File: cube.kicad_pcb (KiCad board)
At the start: 2 copper layers, 282 parts, among them J1 serial_conn, J2 shifters_common_conn, U1 SN74HC595N_0_b, U10 SN74HC595N_3_b, U11 SN74HC595N_3_g, U12 SN74HC595N_3_r, U13 SN74HC595N_4_b, U14 SN74HC595N_4_g, U15 SN74HC595N_4_r, U16 SN74HC595N_5_b, U17 SN74HC595N_5_g, U18 SN74HC595N_5_r, U19 SN74HC595N_6_b, U2 SN74HC595N_0_g, U20 SN74HC595N_6_g, U21 SN74HC595N_6_r, U22 SN74HC595N_7_b, U23 SN74HC595N_7_g, U24 SN74HC595N_7_r, U3 SN74HC595N_0_r, U4 SN74HC595N_1_b, U5 SN74HC595N_1_g, U6 SN74HC595N_1_r, U7 SN74HC595N_2_b, U8 SN74HC595N_2_g, U9 SN74HC595N_2_r

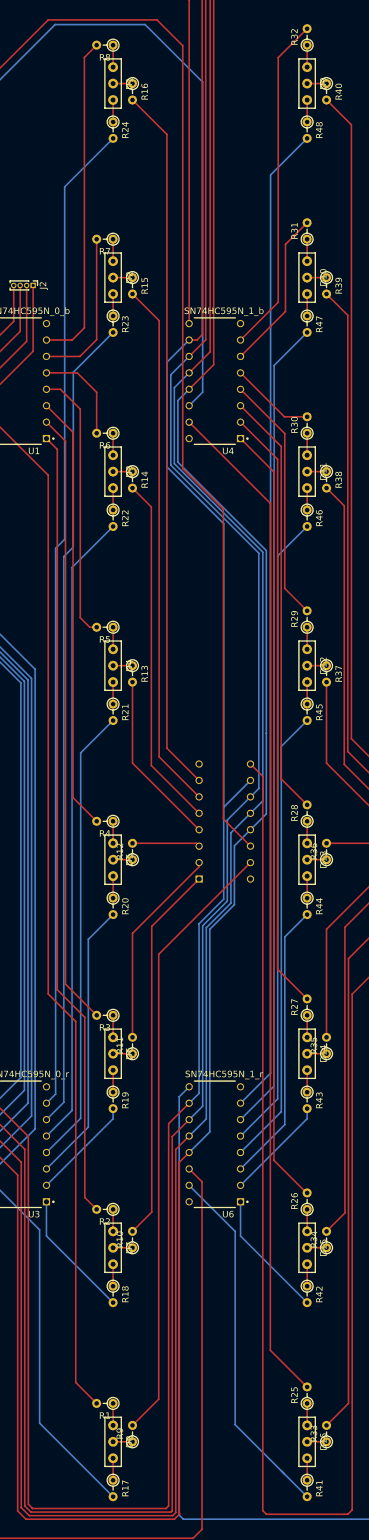
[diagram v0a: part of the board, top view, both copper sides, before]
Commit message: replace led pads on 1st row, fix its red conns
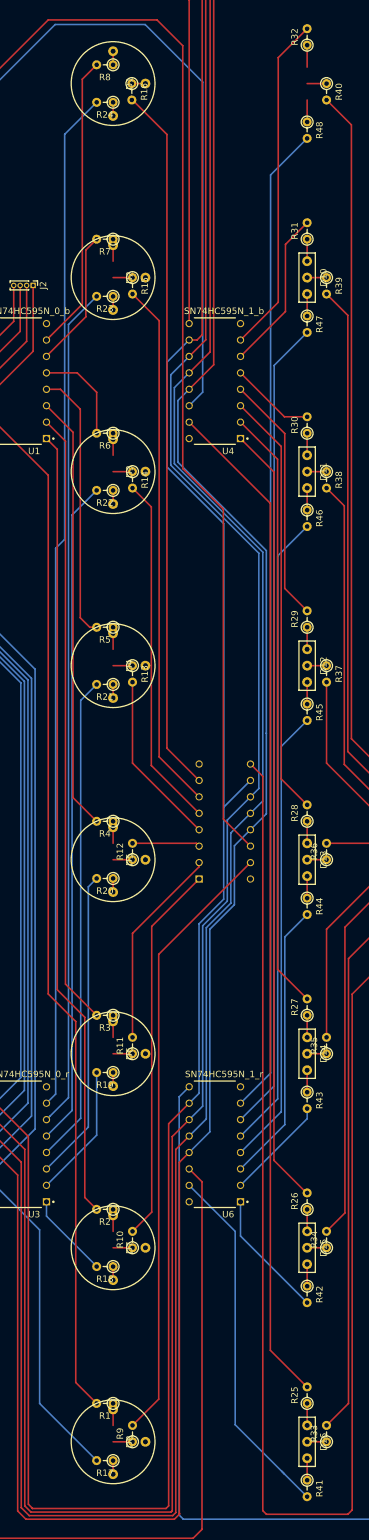
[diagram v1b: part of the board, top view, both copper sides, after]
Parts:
- removed D9: led_1_0, cube:led_pad
- moved R17 3.04 mm to (40.0, 302.9), turned to 180 degrees
- moved R18 3.04 mm to (40.0, 272.9), turned to 180 degrees
- moved R19 3.04 mm to (40.0, 242.9), turned to 180 degrees
- moved R20 3.04 mm to (40.0, 212.9), turned to 180 degrees
- moved R21 3.04 mm to (40.0, 182.9), turned to 180 degrees
- moved R22 3.04 mm to (40.0, 152.9), turned to 180 degrees
- moved R23 3.04 mm to (40.0, 122.9), turned to 180 degrees
- moved R24 3.04 mm to (40.0, 92.9), turned to 180 degrees
- moved R8 3.04 mm to (40.0, 87.1)
- moved R16 0.10 mm to (42.9, 90.0)
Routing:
- net Net-(R18-Pad2): track 19.9 -> 13.2 mm
- net Net-(R17-Pad2): track 55.7 -> 49.1 mm
- net Net-(R8-Pad2): track 51.1 -> 45.8 mm
- net Net-(R21-Pad2): track 71.1 -> 75.6 mm
- net Net-(R20-Pad2): track 43.6 -> 48.1 mm
- net Net-(R24-Pad2): track 153.4 -> 158.0 mm
- net Net-(R22-Pad2): track 98.5 -> 103.0 mm
- net Net-(R19-Pad2): track 16.1 -> 20.7 mm
- net Net-(R23-Pad2): track 126.0 -> 130.5 mm
- net Net-(R7-Pad2): track 24.4 -> 21.3 mm
- net led_0_5_r: track 3.40 -> 2.10 mm
- net led_0_4_r: track 3.40 -> 2.10 mm
- net led_0_3_r: track 3.40 -> 2.10 mm
- net led_0_2_r: track 3.40 -> 2.10 mm
- net led_0_1_r: track 3.40 -> 2.10 mm
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
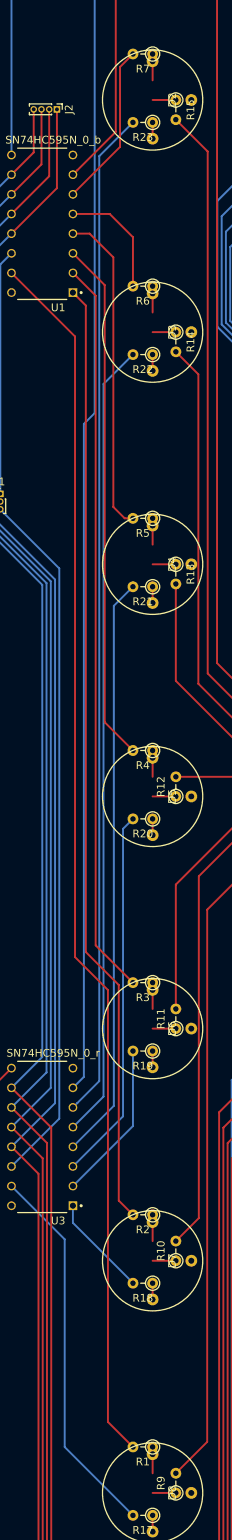
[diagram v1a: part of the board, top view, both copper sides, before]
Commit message: fix 1s rows's blue conns
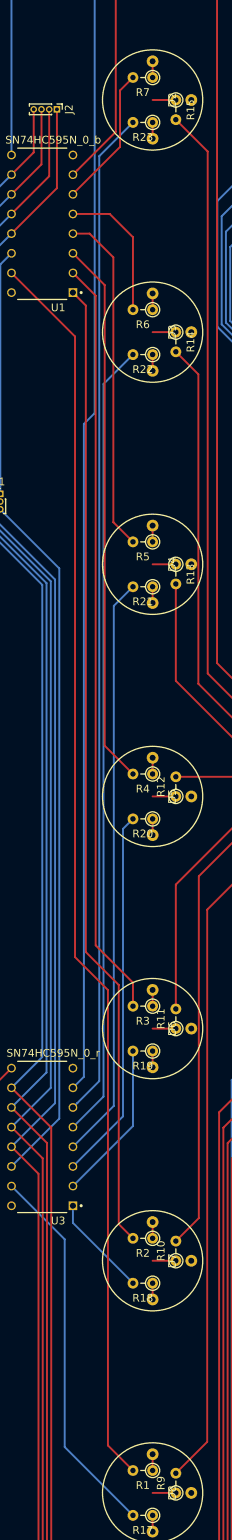
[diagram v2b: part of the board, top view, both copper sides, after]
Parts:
- moved R1 3.04 mm to (40.0, 297.1)
- moved R2 3.04 mm to (40.0, 267.1)
- moved R3 3.04 mm to (40.0, 237.1)
- moved R4 3.04 mm to (40.0, 207.1)
- moved R5 3.04 mm to (40.0, 177.1)
- moved R6 3.04 mm to (40.0, 147.1)
- moved R7 3.04 mm to (40.0, 117.1)
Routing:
- net Net-(R2-Pad2): track 122.4 -> 125.4 mm
- net Net-(R1-Pad2): track 158.3 -> 161.4 mm
- net Net-(R7-Pad2): track 21.3 -> 18.3 mm
- net Net-(R6-Pad2): track 15.3 -> 18.4 mm
- net Net-(R3-Pad2): track 94.9 -> 98.0 mm
- net Net-(R4-Pad2): track 67.5 -> 70.5 mm
- net Net-(R5-Pad2): track 41.9 -> 44.3 mm
- net led_0_5_b: track 3.40 -> 2.10 mm
- net led_0_4_b: track 3.40 -> 2.10 mm
- net led_0_3_b: track 3.40 -> 2.10 mm
- net led_0_2_b: track 3.40 -> 2.10 mm
- net led_0_1_b: track 3.40 -> 2.10 mm
- net led_0_7_b: track 3.40 -> 2.10 mm
- net led_0_6_b: track 3.40 -> 2.10 mm

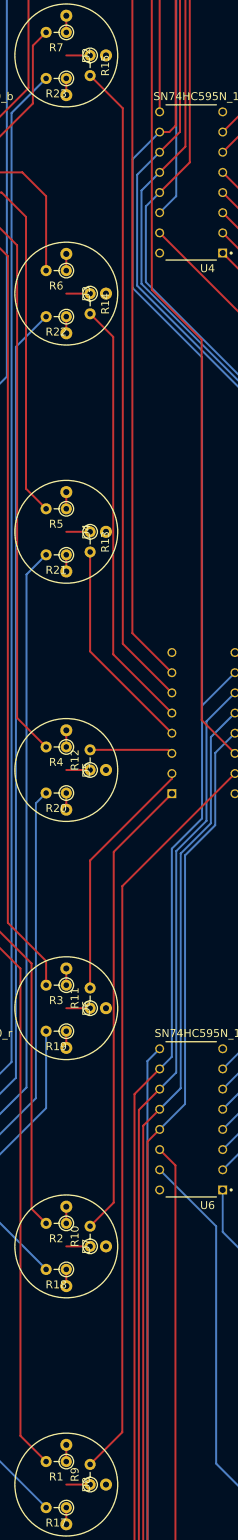
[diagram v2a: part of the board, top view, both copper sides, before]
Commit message: fix 1s rows's green conns
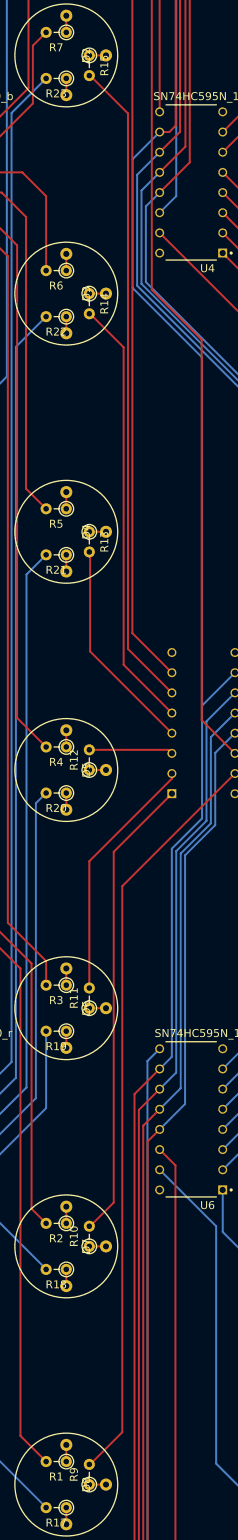
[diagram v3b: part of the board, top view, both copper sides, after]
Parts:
- moved R10 0.10 mm to (42.9, 270.0)
- moved R11 0.10 mm to (42.9, 240.0)
- moved R12 0.10 mm to (42.9, 210.0)
- moved R13 0.10 mm to (42.9, 180.0)
- moved R14 0.10 mm to (42.9, 150.0)
- moved R15 0.10 mm to (42.9, 120.0)
- moved R9 0.10 mm to (42.9, 300.0)
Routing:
- net led_0_7_g: track 3.00 -> 2.10 mm
- net led_0_6_g: track 3.00 -> 2.10 mm
- net led_0_5_g: track 3.00 -> 2.10 mm
- net led_0_4_g: track 3.00 -> 2.10 mm
- net led_0_3_g: track 3.00 -> 2.10 mm
- net led_0_2_g: track 3.00 -> 2.10 mm
- net led_0_1_g: track 3.00 -> 2.10 mm
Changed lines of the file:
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@@
     (thickness 1.6)
     (drawings 0)
-    (tracks 1516)
+    (tracks 1517)
     (zones 0)
     (modules 281)
@@
   )
   (module Resistor_THT:R_Axial_DIN0204_L3.6mm_D1.6mm_P2.54mm_Vertical (layer F.Cu)
-    (at 43 120 270)
+    (at 42.9 120 270)
     (descr "Resistor, Axial_DIN0204 series, Axial, Vertical, pin pitch=2.54mm, 0.167W, length*diameter=3.6*1.6mm^2, http://cdn-reichelt.de/documents/datenblatt/B400/1_4W%23YAG.pdf")
     (tags "Resistor Axial_DIN0204 series Axial Vertical pin pitch 2.54mm 0.167W length 3.6mm diameter 1.6mm")
@@
   )
   (module Resistor_THT:R_Axial_DIN0204_L3.6mm_D1.6mm_P2.54mm_Vertical (layer F.Cu)
-    (at 43 300 90)
+    (at 42.9 300 90)
     (descr "Resistor, Axial_DIN0204 series, Axial, Vertical, pin pitch=2.54mm, 0.167W, length*diameter=3.6*1.6mm^2, http://cdn-reichelt.de/documents/datenblatt/B400/1_4W%23YAG.pdf")
     (tags "Resistor Axial_DIN0204 series Axial Vertical pin pitch 2.54mm 0.167W length 3.6mm diameter 1.6mm")
@@
   )
   (module Resistor_THT:R_Axial_DIN0204_L3.6mm_D1.6mm_P2.54mm_Vertical (layer F.Cu)
-    (at 43 240 90)
+    (at 42.9 240 90)
     (descr "Resistor, Axial_DIN0204 series, Axial, Vertical, pin pitch=2.54mm, 0.167W, length*diameter=3.6*1.6mm^2, http://cdn-reichelt.de/documents/datenblatt/B400/1_4W%23YAG.pdf")
     (tags "Resistor Axial_DIN0204 series Axial Vertical pin pitch 2.54mm 0.167W length 3.6mm diameter 1.6mm")
@@
   )
   (module Resistor_THT:R_Axial_DIN0204_L3.6mm_D1.6mm_P2.54mm_Vertical (layer F.Cu)
-    (at 43 210 90)
+    (at 42.9 210 90)
     (descr "Resistor, Axial_DIN0204 series, Axial, Vertical, pin pitch=2.54mm, 0.167W, length*diameter=3.6*1.6mm^2, http://cdn-reichelt.de/documents/datenblatt/B400/1_4W%23YAG.pdf")
     (tags "Resistor Axial_DIN0204 series Axial Vertical pin pitch 2.54mm 0.167W length 3.6mm diameter 1.6mm")
@@
   )
   (module Resistor_THT:R_Axial_DIN0204_L3.6mm_D1.6mm_P2.54mm_Vertical (layer F.Cu)
-    (at 43 270 90)
+    (at 42.9 270 90)
     (descr "Resistor, Axial_DIN0204 series, Axial, Vertical, pin pitch=2.54mm, 0.167W, length*diameter=3.6*1.6mm^2, http://cdn-reichelt.de/documents/datenblatt/B400/1_4W%23YAG.pdf")
     (tags "Resistor Axial_DIN0204 series Axial Vertical pin pitch 2.54mm 0.167W length 3.6mm diameter 1.6mm")
@@
   )
   (module Resistor_THT:R_Axial_DIN0204_L3.6mm_D1.6mm_P2.54mm_Vertical (layer F.Cu)
-    (at 43 180 270)
+    (at 42.9 180 270)
     (descr "Resistor, Axial_DIN0204 series, Axial, Vertical, pin pitch=2.54mm, 0.167W, length*diameter=3.6*1.6mm^2, http://cdn-reichelt.de/documents/datenblatt/B400/1_4W%23YAG.pdf")
     (tags "Resistor Axial_DIN0204 series Axial Vertical pin pitch 2.54mm 0.167W length 3.6mm diameter 1.6mm")
@@
   )
   (module Resistor_THT:R_Axial_DIN0204_L3.6mm_D1.6mm_P2.54mm_Vertical (layer F.Cu)
-    (at 43 150 270)
+    (at 42.9 150 270)
     (descr "Resistor, Axial_DIN0204 series, Axial, Vertical, pin pitch=2.54mm, 0.167W, length*diameter=3.6*1.6mm^2, http://cdn-reichelt.de/documents/datenblatt/B400/1_4W%23YAG.pdf")
     (tags "Resistor Axial_DIN0204 series Axial Vertical pin pitch 2.54mm 0.167W length 3.6mm diameter 1.6mm")
@@
   (segment (start 40 95) (end 40 92.9) (width 0.25) (layer F.Cu) (net 3))
   (segment (start 40 117.1) (end 40 115) (width 0.25) (layer F.Cu) (net 4))
-  (segment (start 40 120) (end 43 120) (width 0.25) (layer F.Cu) (net 5))
+  (segment (start 42.9 120) (end 45 120) (width 0.25) (layer F.Cu) (net 5))
   (segment (start 40 125) (end 40 122.9) (width 0.25) (layer F.Cu) (net 6))
   (segment (start 40 147.1) (end 40 145) (width 0.25) (layer F.Cu) (net 7))
-  (segment (start 43 150) (end 40 150) (width 0.25) (layer F.Cu) (net 8))
+  (segment (start 42.9 150) (end 45 150) (width 0.25) (layer F.Cu) (net 8))
   (segment (start 40 155) (end 40 152.9) (width 0.25) (layer F.Cu) (net 9))
   (segment (start 40 177.1) (end 40 175) (width 0.25) (layer F.Cu) (net 10))
-  (segment (start 43 180) (end 40 180) (width 0.25) (layer F.Cu) (net 11))
+  (segment (start 42.9 180) (end 45 180) (width 0.25) (layer F.Cu) (net 11))
   (segment (start 40 185) (end 40 182.9) (width 0.25) (layer F.Cu) (net 12))
   (segment (start 40 207.1) (end 40 205) (width 0.25) (layer F.Cu) (net 13))
-  (segment (start 43 210) (end 40 210) (width 0.25) (layer F.Cu) (net 14))
+  (segment (start 45 210) (end 42.9 210) (width 0.25) (layer F.Cu) (net 14))
   (segment (start 40 215) (end 40 212.9) (width 0.25) (layer F.Cu) (net 15))
   (segment (start 40 237.1) (end 40 235) (width 0.25) (layer F.Cu) (net 16))
-  (segment (start 43 240) (end 40 240) (width 0.25) (layer F.Cu) (net 17))
+  (segment (start 45 240) (end 42.9 240) (width 0.25) (layer F.Cu) (net 17))
   (segment (start 40 245) (end 40 242.9) (width 0.25) (layer F.Cu) (net 18))
   (segment (start 40 267.1) (end 40 265) (width 0.25) (layer F.Cu) (net 19))
-  (segment (start 40 270) (end 43 270) (width 0.25) (layer F.Cu) (net 20))
+  (segment (start 42.9 270) (end 45 270) (width 0.25) (layer F.Cu) (net 20))
   (segment (start 40 275) (end 40 272.9) (width 0.25) (layer F.Cu) (net 21))
   (segment (start 40 297.1) (end 40 295) (width 0.25) (layer F.Cu) (net 22))
-  (segment (start 40 300) (end 43 300) (width 0.25) (layer F.Cu) (net 23))
+  (segment (start 42.9 300) (end 45 300) (width 0.25) (layer F.Cu) (net 23))
   (segment (start 40 305) (end 40 302.9) (width 0.25) (layer F.Cu) (net 24))
   (segment (start 27.94 180.5432) (end 27.94 251.63) (width 0.25) (layer B.Cu) (net 25))
@@
   (segment (start 43 267.46) (end 45.974 264.486) (width 0.25) (layer F.Cu) (net 73))
   (segment (start 53.3 211.089998) (end 53.3 210.445) (width 0.25) (layer F.Cu) (net 74))
-  (segment (start 43 221.389998) (end 53.3 211.089998) (width 0.25) (layer F.Cu) (net 74))
-  (segment (start 43 237.46) (end 43 221.389998) (width 0.25) (layer F.Cu) (net 74))
+  (segment (start 42.9 221.489998) (end 53.3 211.089998) (width 0.25) (layer F.Cu) (net 74))
+  (segment (start 42.9 237.36) (end 42.9 221.489998) (width 0.25) (layer F.Cu) (net 74))
+  (segment (start 43 237.46) (end 42.9 237.36) (width 0.25) (layer F.Cu) (net 74))
   (segment (start 52.855 207.46) (end 53.3 207.905) (width 0.25) (layer F.Cu) (net 75))
   (segment (start 43 207.46) (end 52.855 207.46) (width 0.25) (layer F.Cu) (net 75))
   (segment (start 43 195.065) (end 53.3 205.365) (width 0.25) (layer F.Cu) (net 76))
   (segment (start 43 182.54) (end 43 195.065) (width 0.25) (layer F.Cu) (net 76))
-  (segment (start 45.9105 195.4355) (end 53.3 202.825) (width 0.25) (layer F.Cu) (net 77))
-  (segment (start 45.9105 155.4505) (end 45.9105 195.4355) (width 0.25) (layer F.Cu) (net 77))
-  (segment (start 43 152.54) (end 45.9105 155.4505) (width 0.25) (layer F.Cu) (net 77))
-  (segment (start 47.117 194.102) (end 53.3 200.285) (width 0.25) (layer F.Cu) (net 78))
-  (segment (start 47.117 126.657) (end 47.117 194.102) (width 0.25) (layer F.Cu) (net 78))
-  (segment (start 43 122.54) (end 47.117 126.657) (width 0.25) (layer F.Cu) (net 78))
+  (segment (start 47.2186 156.7586) (end 47.2186 196.7436) (width 0.25) (layer F.Cu) (net 77))
+  (segment (start 43 152.54) (end 47.2186 156.7586) (width 0.25) (layer F.Cu) (net 77))
+  (segment (start 47.2186 196.7436) (end 53.3 202.825) (width 0.25) (layer F.Cu) (net 77))
+  (segment (start 47.768611 194.753611) (end 53.3 200.285) (width 0.25) (layer F.Cu) (net 78))
+  (segment (start 47.768611 127.308611) (end 47.768611 194.753611) (width 0.25) (layer F.Cu) (net 78))
+  (segment (start 43 122.54) (end 47.768611 127.308611) (width 0.25) (layer F.Cu) (net 78))
   (segment (start 48.3235 192.7685) (end 53.3 197.745) (width 0.25) (layer F.Cu) (net 79))
   (segment (start 48.3235 97.8635) (end 48.3235 192.7685) (width 0.25) (layer F.Cu) (net 79))

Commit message: fix 2nd rows's red conns
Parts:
- added D9: led_1_0, cube:led_pad, F.Cu at (70.0, 90.0)
- added J10: Conn_01x01, Connector_Pin:Pin_D0.7mm_L6.5mm_W1.8mm_FlatFork, F.Cu at (97.4, 61.8)
- added J11: Conn_01x01, Connector_Pin:Pin_D0.7mm_L6.5mm_W1.8mm_FlatFork, F.Cu at (93.6, 61.8)
- added J3: Conn_01x01, Connector_Pin:Pin_D0.7mm_L6.5mm_W1.8mm_FlatFork, F.Cu at (127.7, 50.9)
- added J4: Conn_01x01, Connector_Pin:Pin_D0.7mm_L6.5mm_W1.8mm_FlatFork, F.Cu at (131.5, 47.4)
- added J5: Conn_01x01, Connector_Pin:Pin_D0.7mm_L6.5mm_W1.8mm_FlatFork, F.Cu at (131.5, 44.0)
- added J6: Conn_01x01, Connector_Pin:Pin_D0.7mm_L6.5mm_W1.8mm_FlatFork, F.Cu at (127.7, 47.4)
- added J7: Conn_01x01, Connector_Pin:Pin_D0.7mm_L6.5mm_W1.8mm_FlatFork, F.Cu at (131.5, 40.5)
- added J8: Conn_01x01, Connector_Pin:Pin_D0.7mm_L6.5mm_W1.8mm_FlatFork, F.Cu at (127.7, 44.0)
- added J9: Conn_01x01, Connector_Pin:Pin_D0.7mm_L6.5mm_W1.8mm_FlatFork, F.Cu at (127.7, 40.5)
- added Q1: IRF9540N, Package_TO_SOT_THT:TO-220-3_Vertical, F.Cu at (105.9, 42.7)
- added Q2: IRF9540N, Package_TO_SOT_THT:TO-220-3_Vertical, F.Cu at (105.9, 48.7)
- added Q3: IRF9540N, Package_TO_SOT_THT:TO-220-3_Vertical, F.Cu at (117.5, 42.7)
- added Q4: IRF9540N, Package_TO_SOT_THT:TO-220-3_Vertical, F.Cu at (105.9, 54.7)
- added Q5: IRF9540N, Package_TO_SOT_THT:TO-220-3_Vertical, F.Cu at (117.5, 48.7)
- added Q6: IRF9540N, Package_TO_SOT_THT:TO-220-3_Vertical, F.Cu at (105.9, 60.6)
- added Q7: IRF9540N, Package_TO_SOT_THT:TO-220-3_Vertical, F.Cu at (117.5, 54.7)
- added Q8: IRF9540N, Package_TO_SOT_THT:TO-220-3_Vertical, F.Cu at (117.5, 60.6)
- added U25: SN74HC595N_cols, SN74HC595N:DIP794W45P254L1969H508Q16, F.Cu at (97.4, 49.4)
- moved R41 3.04 mm to (70.0, 302.9), turned to 180 degrees
- moved R42 3.04 mm to (70.0, 272.9), turned to 180 degrees
- moved R43 3.04 mm to (70.0, 242.9), turned to 180 degrees
- moved R44 3.04 mm to (70.0, 212.9), turned to 180 degrees
- moved R45 3.04 mm to (70.0, 182.9), turned to 180 degrees
- moved R46 3.04 mm to (70.0, 152.9), turned to 180 degrees
- moved R47 3.04 mm to (70.0, 122.9), turned to 180 degrees
- moved R48 3.04 mm to (70.0, 92.9), turned to 180 degrees
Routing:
- net Net-(R41-Pad2): track 56.3 -> 49.1 mm
- net Net-(R42-Pad2): track 19.9 -> 13.2 mm
- net Net-(R46-Pad2): track 98.5 -> 103.0 mm
- net Net-(R44-Pad2): track 43.6 -> 48.1 mm
- net Net-(R48-Pad2): track 153.4 -> 158.0 mm
- net Net-(R43-Pad2): track 16.1 -> 20.7 mm
- net Net-(R47-Pad2): track 126.0 -> 130.5 mm
- net Net-(R45-Pad2): track 71.1 -> 75.6 mm
- net led_1_5_r: track 3.40 -> 2.10 mm
- net led_1_4_r: track 3.40 -> 2.10 mm
- net led_1_3_r: track 3.40 -> 2.10 mm
- net led_1_2_r: track 3.40 -> 2.10 mm
- net led_1_1_r: track 3.40 -> 2.10 mm
- net led_1_0_r: track 3.40 -> 2.10 mm
- net led_1_7_r: track 3.40 -> 2.10 mm
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
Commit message: fix 2nd rows's blue conns
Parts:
- moved R25 3.04 mm to (70.0, 297.1), turned to 180 degrees
- moved R26 3.04 mm to (70.0, 267.1), turned to 180 degrees
- moved R27 3.04 mm to (70.0, 237.1), turned to 180 degrees
- moved R28 3.04 mm to (70.0, 207.1), turned to 180 degrees
- moved R29 3.04 mm to (70.0, 177.1), turned to 180 degrees
- moved R30 3.04 mm to (70.0, 147.1), turned to 180 degrees
- moved R31 3.04 mm to (70.0, 117.1), turned to 180 degrees
- moved R32 3.04 mm to (70.0, 87.1), turned to 180 degrees
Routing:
- net Net-(R31-Pad2): track 24.9 -> 18.3 mm
- net Net-(R32-Pad2): track 52.4 -> 45.8 mm
- net Net-(R26-Pad2): track 121.4 -> 125.9 mm
- net Net-(R25-Pad2): track 156.7 -> 161.3 mm
- net Net-(R27-Pad2): track 93.4 -> 98.0 mm
- net Net-(R29-Pad2): track 38.5 -> 43.0 mm
- net Net-(R28-Pad2): track 66.0 -> 70.5 mm
- net led_1_0_b: track 3.40 -> 0.00 mm
- net Net-(R30-Pad2): track 13.1 -> 15.6 mm
- net led_1_5_b: track 3.40 -> 2.10 mm
- net led_1_4_b: track 3.40 -> 2.10 mm
- net led_1_3_b: track 3.40 -> 2.10 mm
- net led_1_2_b: track 3.40 -> 2.10 mm
- net led_1_1_b: track 3.40 -> 2.10 mm
- net led_1_7_b: track 3.40 -> 2.10 mm
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
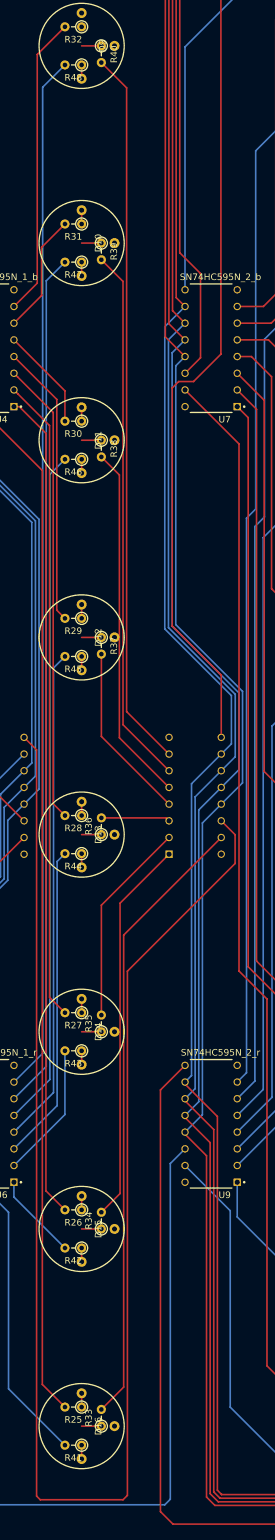
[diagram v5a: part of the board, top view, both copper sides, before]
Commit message: fix 2nd rows's green conns
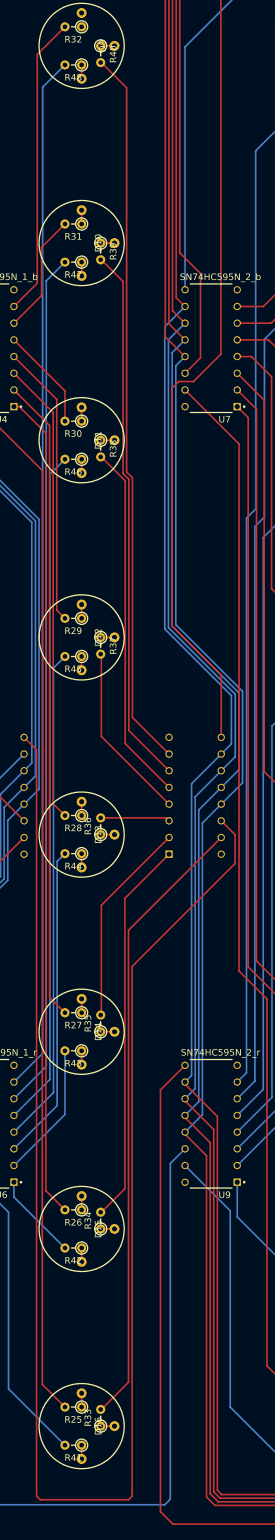
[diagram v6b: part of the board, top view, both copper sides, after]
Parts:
- moved R33 0.10 mm to (72.9, 300.0)
- moved R34 0.10 mm to (72.9, 270.0)
- moved R35 0.10 mm to (72.9, 240.0)
- moved R36 0.10 mm to (72.9, 210.0)
- moved R37 0.10 mm to (72.9, 180.0)
- moved R38 0.10 mm to (72.9, 150.0)
- moved R39 0.10 mm to (72.9, 120.0)
- moved R40 0.10 mm to (72.9, 90.0)
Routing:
- net led_1_7_g: track 3.00 -> 2.10 mm
- net led_1_6_g: track 3.00 -> 2.10 mm
- net led_1_5_g: track 3.00 -> 2.10 mm
- net led_1_4_g: track 3.00 -> 2.10 mm
- net led_1_3_g: track 3.00 -> 2.10 mm
- net led_1_2_g: track 3.00 -> 2.10 mm
- net led_1_1_g: track 3.00 -> 2.10 mm
- net led_1_0_g: track 3.00 -> 2.10 mm
